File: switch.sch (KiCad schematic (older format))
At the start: 2 parts, among them J3 FSA2269, U1 DG419

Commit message: Add part for TS5A22364-Q1 and replace FSA2269 with it.
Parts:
- removed J3: FSA2269, blubaru:FSA2269, symbol FSA2269
- added J?: TS5A22364-Q1, symbol TS5A22364-Q1
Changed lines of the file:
@@
 Wire Wire Line
 	6850 3650 7000 3650
-Text HLabel 5100 4400 2    60   Input ~ 0
+Text HLabel 4300 4750 0    60   Input ~ 0
 L_CD
-Text HLabel 4000 4500 0    60   Input ~ 0
+Text HLabel 5400 4650 2    60   Input ~ 0
 R_CD
 Text HLabel 6150 3600 0    60   Input ~ 0
 TRG_CD
-Text HLabel 4000 4400 0    60   Input ~ 0
+Text HLabel 4300 4550 0    60   Input ~ 0
 BT_L
-Text HLabel 4000 4600 0    60   Input ~ 0
+Text HLabel 5400 4450 2    60   Input ~ 0
 BT_R
 Text HLabel 7650 4750 2    60   Input ~ 0
 BT_TRG
-Text HLabel 5100 4600 2    60   Output ~ 0
+Text HLabel 4300 4650 0    60   Output ~ 0
 L_STEREO
-Text HLabel 4000 4800 0    60   Output ~ 0
+Text HLabel 5400 4550 2    60   Output ~ 0
 R_STEREO
 Text HLabel 7000 3650 2    60   Output ~ 0
 TRG_STEREO
 $Comp
-L FSA2269 J3
-U 1 1 58B3B18B
-P 4550 4300
-F 0 "J3" H 4550 3700 60  0000 C CNN
-F 1 "FSA2269" H 4550 4300 60  0000 C CNN
-F 2 "blubaru:FSA2269" H 4550 4300 60  0001 C CNN
-F 3 "https://www.fairchildsemi.com/datasheets/FS/FSA2269.pdf" H 4550 4300 60  0001 C CNN
-	1    4550 4300
+L GND #PWR08
+U 1 1 58B3B20A
+P 5650 4900
+F 0 "#PWR08" H 5650 4650 50  0001 C CNN
+F 1 "GND" H 5650 4750 50  0000 C CNN
+F 2 "" H 5650 4900 50  0000 C CNN
+F 3 "" H 5650 4900 50  0000 C CNN
+	1    5650 4900
 	1    0    0    -1
 $EndComp
 $Comp
-L GND #PWR08
-U 1 1 58B3B20A
-P 3250 4750
-F 0 "#PWR08" H 3250 4500 50  0001 C CNN
-F 1 "GND" H 3250 4600 50  0000 C CNN
-F 2 "" H 3250 4750 50  0000 C CNN
-F 3 "" H 3250 4750 50  0000 C CNN
-	1    3250 4750
+L VCC #PWR09
+U 1 1 58B3B22E
+P 4100 4350
+F 0 "#PWR09" H 4100 4200 50  0001 C CNN
+F 1 "VCC" H 4100 4500 50  0000 C CNN
+F 2 "" H 4100 4350 50  0000 C CNN
+F 3 "" H 4100 4350 50  0000 C CNN
+	1    4100 4350
 	1    0    0    -1
 $EndComp
 Wire Wire Line
-	4000 4700 3250 4700
-Wire Wire Line
-	3250 4700 3250 4750
-$Comp
-L VCC #PWR09
-U 1 1 58B3B22E
-P 5550 4400
-F 0 "#PWR09" H 5550 4250 50  0001 C CNN
-F 1 "VCC" H 5550 4550 50  0000 C CNN
-F 2 "" H 5550 4400 50  0000 C CNN
-F 3 "" H 5550 4400 50  0000 C CNN
-	1    5550 4400
-	1    0    0    -1
-$EndComp
-Wire Wire Line
-	5100 4500 5550 4500
-Wire Wire Line
-	5550 4500 5550 4400
-Wire Wire Line
 	5400 4750 7650 4750
-Wire Wire Line
-	5100 4700 5400 4700
-Wire Wire Line
-	5400 4700 5400 4800
-Wire Wire Line
-	5400 4800 5100 4800
-Connection ~ 5400 4750
 $Comp
 L DG419 U1
@@
 Wire Wire Line
 	5750 3700 6250 3700
+$Comp
+L TS5A22364-Q1 J?
+U 1 1 59323EF4
+P 4850 4350
+F 0 "J?" H 4850 3750 60  0000 C CNN
+F 1 "TS5A22364-Q1" H 4850 4350 60  0000 C CNN
+F 2 "" H 4850 4350 60  0001 C CNN
+F 3 "" H 4850 4350 60  0001 C CNN
+	1    4850 4350
+	1    0    0    -1
+$EndComp
+Wire Wire Line
+	4100 4350 4100 4450
+Wire Wire Line
+	4100 4450 4300 4450
+Wire Wire Line
+	5650 4900 5650 4850
+Wire Wire Line
+	5650 4850 5400 4850
+Wire Wire Line
+	6000 4750 6000 5250
+Wire Wire Line
+	6000 5250 4300 5250
+Wire Wire Line
+	4300 5250 4300 4850
+Connection ~ 6000 4750
 $EndSCHEMATC

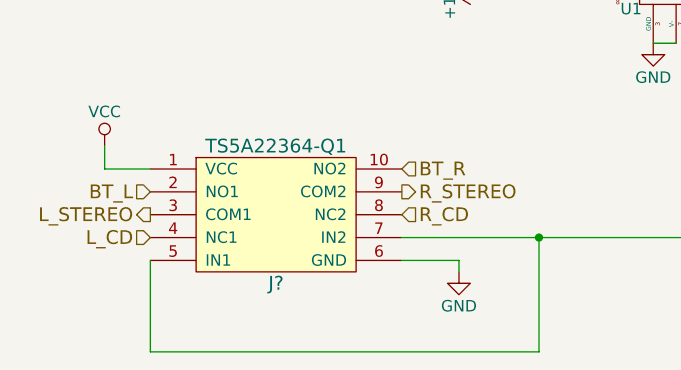
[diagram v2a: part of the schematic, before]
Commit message: Add footprints for audio switch and amp.
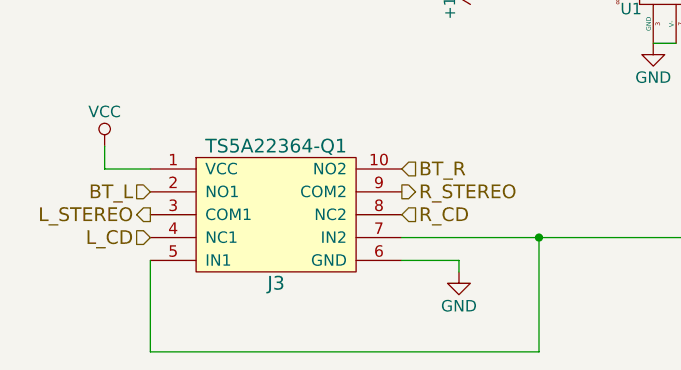
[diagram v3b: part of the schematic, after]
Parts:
- J3: renamed from J?; footprint (none) -> blubaru:TS5A22364-Q1
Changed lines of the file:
@@
 	5750 3700 6250 3700
 $Comp
-L TS5A22364-Q1 J?
+L TS5A22364-Q1 J3
 U 1 1 59323EF4
 P 4850 4350
-F 0 "J?" H 4850 3750 60  0000 C CNN
+F 0 "J3" H 4850 3750 60  0000 C CNN
 F 1 "TS5A22364-Q1" H 4850 4350 60  0000 C CNN
-F 2 "" H 4850 4350 60  0001 C CNN
+F 2 "blubaru:TS5A22364-Q1" H 4850 4350 60  0001 C CNN
 F 3 "" H 4850 4350 60  0001 C CNN
 	1    4850 4350

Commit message: Add resistor values to LEDs and a voltage regulator. Has power pin errors still.
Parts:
- renumbered U1 to U2
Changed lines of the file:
@@
 TRG_STEREO
 $Comp
-L GND #PWR7
+L GND #PWR010
 U 1 1 58B3B20A
 P 5650 4900
-F 0 "#PWR7" H 5650 4650 50  0001 C CNN
+F 0 "#PWR010" H 5650 4650 50  0001 C CNN
 F 1 "GND" H 5650 4750 50  0000 C CNN
 F 2 "" H 5650 4900 50  0000 C CNN
@@
 $EndComp
 $Comp
-L VCC #PWR6
+L VCC #PWR011
 U 1 1 58B3B22E
 P 4100 4350
-F 0 "#PWR6" H 4100 4200 50  0001 C CNN
+F 0 "#PWR011" H 4100 4200 50  0001 C CNN
 F 1 "VCC" H 4100 4500 50  0000 C CNN
 F 2 "" H 4100 4350 50  0000 C CNN
@@
 	5400 4750 7650 4750
 $Comp
-L DG419 U1
+L DG419 U2
 U 1 1 58B47B5A
 P 6550 3650
-F 0 "U1" H 6650 3550 50  0000 L CNN
+F 0 "U2" H 6650 3550 50  0000 L CNN
 F 1 "DG419" H 6650 3750 50  0000 L CNN
 F 2 "Housings_DIP:DIP-8_W7.62mm" H 6550 3650 60  0001 C CNN
@@
 $EndComp
 $Comp
-L GND #PWR10
+L GND #PWR012
 U 1 1 58B47DD4
 P 6500 3900
-F 0 "#PWR10" H 6500 3650 50  0001 C CNN
+F 0 "#PWR012" H 6500 3650 50  0001 C CNN
 F 1 "GND" H 6500 3750 50  0000 C CNN
 F 2 "" H 6500 3900 50  0000 C CNN
@@
 $EndComp
 $Comp
-L +12V #PWR11
+L +12V #PWR013
 U 1 1 58B47DEE
 P 6600 3250
-F 0 "#PWR11" H 6600 3100 50  0001 C CNN
+F 0 "#PWR013" H 6600 3100 50  0001 C CNN
 F 1 "+12V" H 6600 3390 50  0000 C CNN
 F 2 "" H 6600 3250 50  0000 C CNN
@@
 	6600 3250 6600 3400
 $Comp
-L VCC #PWR9
+L VCC #PWR014
 U 1 1 58B483A9
 P 6500 3400
-F 0 "#PWR9" H 6500 3250 50  0001 C CNN
+F 0 "#PWR014" H 6500 3250 50  0001 C CNN
 F 1 "VCC" H 6500 3550 50  0000 C CNN
 F 2 "" H 6500 3400 50  0000 C CNN
@@
 $EndComp
 $Comp
-L +12V #PWR8
+L +12V #PWR015
 U 1 1 58B4A9F8
 P 5750 3700
-F 0 "#PWR8" H 5750 3550 50  0001 C CNN
+F 0 "#PWR015" H 5750 3550 50  0001 C CNN
 F 1 "+12V" H 5750 3840 50  0000 C CNN
 F 2 "" H 5750 3700 50  0000 C CNN

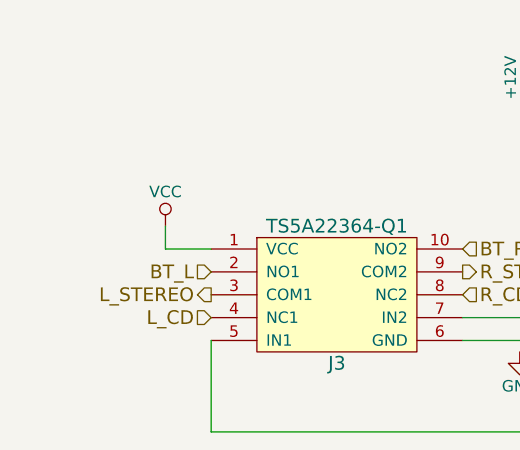
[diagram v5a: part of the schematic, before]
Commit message: Voltage regulator adjustments and tidying
Switch to LD1117 component and add decoupling caps.
Add a decoupling cap to the audio switch
Shift some status LEDs to modules layer
Use ProMini instead of ProMicro
Update BOM
Update netlist
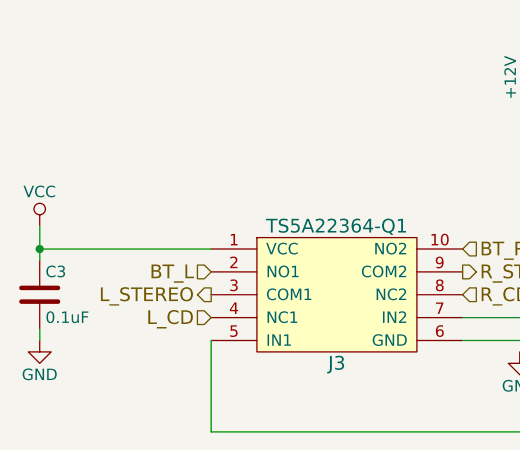
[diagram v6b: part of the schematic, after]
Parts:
- added C3: 0.1uF, blubaru:C_Disc_D5.5mm_W2.5mm_P2.50mm, symbol C
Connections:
- net GND: now also C3.2
- net VCC: now also C3.1
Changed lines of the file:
@@
 TRG_STEREO
 $Comp
-L GND #PWR010
+L GND #PWR011
 U 1 1 58B3B20A
 P 5650 4900
-F 0 "#PWR010" H 5650 4650 50  0001 C CNN
+F 0 "#PWR011" H 5650 4650 50  0001 C CNN
 F 1 "GND" H 5650 4750 50  0000 C CNN
 F 2 "" H 5650 4900 50  0000 C CNN
@@
 $EndComp
 $Comp
-L VCC #PWR011
+L VCC #PWR012
 U 1 1 58B3B22E
-P 4100 4350
-F 0 "#PWR011" H 4100 4200 50  0001 C CNN
-F 1 "VCC" H 4100 4500 50  0000 C CNN
-F 2 "" H 4100 4350 50  0000 C CNN
-F 3 "" H 4100 4350 50  0000 C CNN
-	1    4100 4350
+P 3550 4350
+F 0 "#PWR012" H 3550 4200 50  0001 C CNN
+F 1 "VCC" H 3550 4500 50  0000 C CNN
+F 2 "" H 3550 4350 50  0000 C CNN
+F 3 "" H 3550 4350 50  0000 C CNN
+	1    3550 4350
 	1    0    0    -1
 $EndComp
@@
 $EndComp
 $Comp
-L GND #PWR012
+L GND #PWR013
 U 1 1 58B47DD4
 P 6500 3900
-F 0 "#PWR012" H 6500 3650 50  0001 C CNN
+F 0 "#PWR013" H 6500 3650 50  0001 C CNN
 F 1 "GND" H 6500 3750 50  0000 C CNN
 F 2 "" H 6500 3900 50  0000 C CNN
@@
 $EndComp
 $Comp
-L +12V #PWR013
+L +12V #PWR014
 U 1 1 58B47DEE
 P 6600 3250
-F 0 "#PWR013" H 6600 3100 50  0001 C CNN
+F 0 "#PWR014" H 6600 3100 50  0001 C CNN
 F 1 "+12V" H 6600 3390 50  0000 C CNN
 F 2 "" H 6600 3250 50  0000 C CNN
@@
 	6600 3250 6600 3400
 $Comp
-L VCC #PWR014
+L VCC #PWR015
 U 1 1 58B483A9
 P 6500 3400
-F 0 "#PWR014" H 6500 3250 50  0001 C CNN
+F 0 "#PWR015" H 6500 3250 50  0001 C CNN
 F 1 "VCC" H 6500 3550 50  0000 C CNN
 F 2 "" H 6500 3400 50  0000 C CNN
@@
 $EndComp
 $Comp
-L +12V #PWR015
+L +12V #PWR016
 U 1 1 58B4A9F8
 P 5750 3700
-F 0 "#PWR015" H 5750 3550 50  0001 C CNN
+F 0 "#PWR016" H 5750 3550 50  0001 C CNN
 F 1 "+12V" H 5750 3840 50  0000 C CNN
 F 2 "" H 5750 3700 50  0000 C CNN
@@
 F 1 "TS5A22364-Q1" H 4850 4350 60  0000 C CNN
 F 2 "blubaru:TS5A22364-Q1" H 4850 4350 60  0001 C CNN
-F 3 "" H 4850 4350 60  0001 C CNN
+F 3 "http://www.ti.com/lit/ds/symlink/ts5a22364-q1.pdf" H 4850 4350 60  0001 C CNN
 	1    4850 4350
 	1    0    0    -1
 $EndComp
 Wire Wire Line
-	4100 4350 4100 4450
+	3550 4350 3550 4500
 Wire Wire Line
-	4100 4450 4300 4450
+	3550 4450 4300 4450
 Wire Wire Line
 	5650 4900 5650 4850
@@
 	4300 5250 4300 4850
 Connection ~ 6000 4750
+$Comp
+L C C3
+U 1 1 594EA706
+P 3550 4650
+F 0 "C3" H 3575 4750 50  0000 L CNN
+F 1 "0.1uF" H 3575 4550 50  0000 L CNN
+F 2 "blubaru:C_Disc_D5.5mm_W2.5mm_P2.50mm" H 3588 4500 50  0001 C CNN
+F 3 "" H 3550 4650 50  0001 C CNN
+	1    3550 4650
+	1    0    0    -1
+$EndComp
+$Comp
+L GND #PWR017
+U 1 1 594EA72E
+P 3550 4850
+F 0 "#PWR017" H 3550 4600 50  0001 C CNN
+F 1 "GND" H 3550 4700 50  0000 C CNN
+F 2 "" H 3550 4850 50  0001 C CNN
+F 3 "" H 3550 4850 50  0001 C CNN
+	1    3550 4850
+	1    0    0    -1
+$EndComp
+Connection ~ 3550 4450
+Wire Wire Line
+	3550 4800 3550 4850
 $EndSCHEMATC

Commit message: Add new capacitor footprints and associate them.
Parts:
- C3: footprint blubaru:C_Disc_D5.5mm_W2.5mm_P2.50mm -> blubaru:C_Disc_D4.0mm_W2.6mm_P2.50mm
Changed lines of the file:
@@
 F 0 "C3" H 3575 4750 50  0000 L CNN
 F 1 "0.1uF" H 3575 4550 50  0000 L CNN
-F 2 "blubaru:C_Disc_D5.5mm_W2.5mm_P2.50mm" H 3588 4500 50  0001 C CNN
+F 2 "blubaru:C_Disc_D4.0mm_W2.6mm_P2.50mm" H 3588 4500 50  0001 C CNN
 F 3 "" H 3550 4650 50  0001 C CNN
 	1    3550 4650
